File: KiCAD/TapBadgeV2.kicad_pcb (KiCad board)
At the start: 4 copper layers, 44 x 52.4 mm, 83 parts, among them J201 Conn_02x04_Counter_Clockwise, J301 UJC-HP-3-SMT-TR, M101 G0832013D, SW302 KXT 331 LHS, U101 DRV2605, U201 ESP32-PICO-D4, U401 BME680, U402 APDS-9500, U403 LSM6DSM, U404 CMM-4030D-261-I2S-TR, U405 TSOP75340TTCT-ND, U406 MAX86150EFF+T, U407 VL6180XV0NR_1, U408 LP5907MFX-2.8

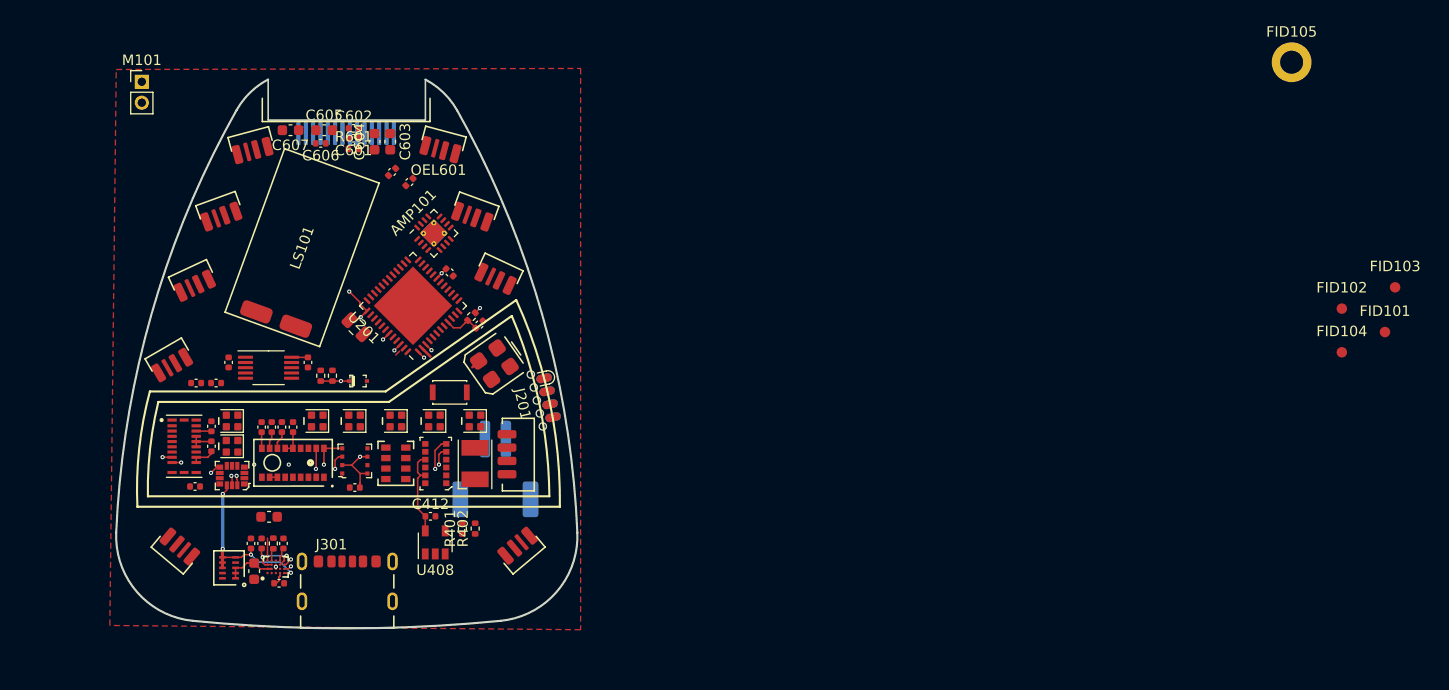
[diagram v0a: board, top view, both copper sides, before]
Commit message: Continue work on Schematics
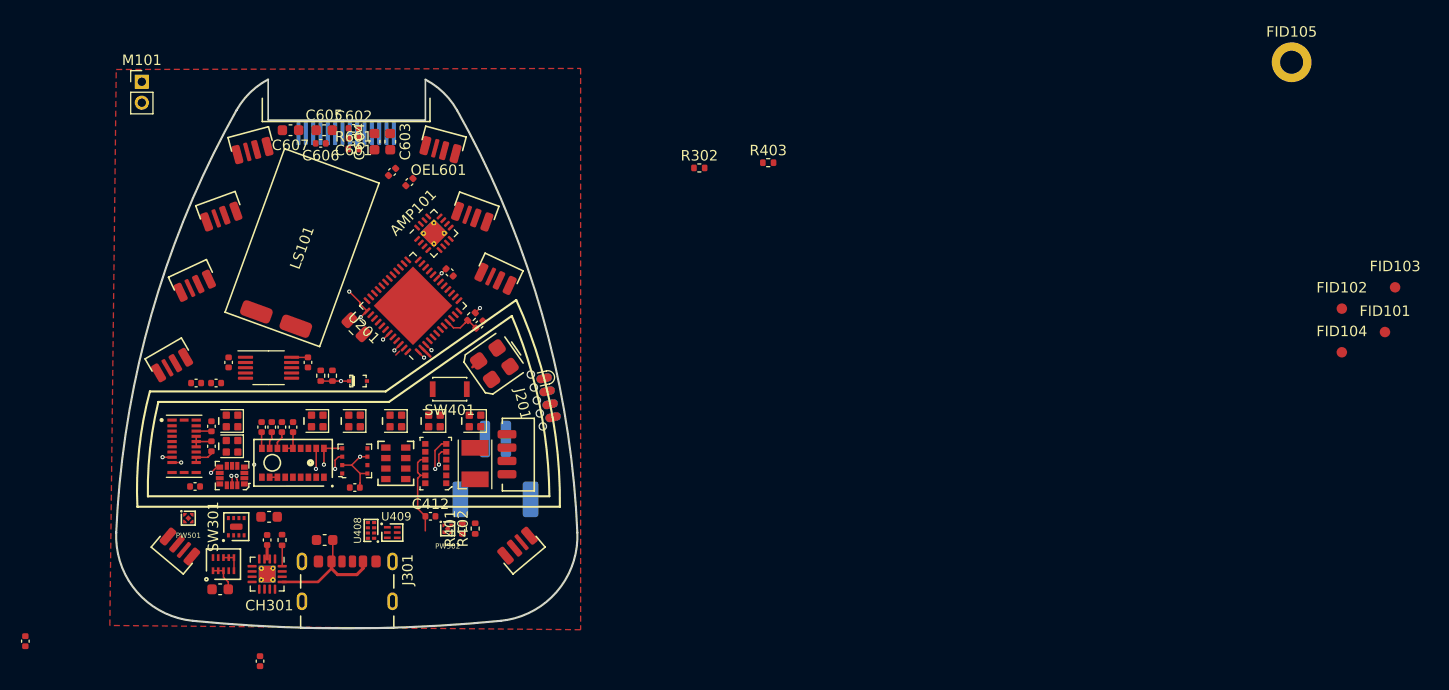
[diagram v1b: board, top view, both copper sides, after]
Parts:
- removed BC301: BQ25157, XasPrints:DSBGA-20
- removed FID301: Fiducial, XasPrints:LiPo_150mAh
- removed SW302: KXT 331 LHS, Button_Switch_SMD:SW_SPST_CK_KXT3
- added CH301: BQ24232, Package_DFN_QFN:VQFN-16-1EP_3x3mm_P0.5mm_EP1.6x1.6mm_ThermalVias, F.Cu at (92.4, 106.3)
- added PW501: AP7354-18FS4, XasPrints:X2-DFN1010-4, F.Cu at (84.9, 101.0)
- added PW502: AP7354-28FS4, XasPrints:X2-DFN1010-4, F.Cu at (109.6, 102.0)
- added R302: 10k 0402, Resistor_SMD:R_0402_1005Metric, F.Cu at (133.6, 67.6)
- added R403: 900k 0402, Resistor_SMD:R_0402_1005Metric, F.Cu at (140.2, 67.1)
- added SW301: MIC94069, XasPrints:MLF-6-EP-P0.5mm, F.Cu at (89.5, 101.8)
- added SW401: KXT 331 LHS, Button_Switch_SMD:SW_SPST_CK_KXT3, F.Cu at (109.8, 88.7)
- added U409: SR1PBBU, XasPrints:UDFN6, F.Cu at (104.3, 102.3)
- C303: value 2.2uF 0402 -> 1uF 0603 16V; footprint Capacitor_SMD:C_0402_1005Metric -> Capacitor_SMD:C_0603_1608Metric
- R301: value 5k 0402 -> 10k 0402
- U408: value LP5907MFX-2.8 -> 74LVC1G74GT-Q100X; footprint Package_TO_SOT_SMD:SOT-23-5 -> XasPrints:XSON8
- moved C305 23.5 mm to (69.3, 112.7), turned to 270 degrees
- moved C304 11.4 mm to (91.7, 114.6)
- moved U408 6.23 mm to (102.3, 102.1)
- moved C303 6.00 mm to (97.9, 103.0), turned to 180 degrees
- moved C302 3.68 mm to (87.9, 107.8), turned to 180 degrees
- moved R301 0.89 mm to (93.8, 103.0)
- moved PW301 0.63 mm to (88.2, 105.4), turned to 0 degrees
- moved C301 0.62 mm to (92.4, 103.0)
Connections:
- net +1V8 renamed Net-(C408-Pad1)
- C101 pad 2: +BATT -> +5V
- C302 pad 1: +BATT -> +5V
- C303 pad 1: Net-(BC301-PadD1) -> Net-(C303-Pad1)
- C304 pad 1: VGLOW -> Net-(C304-Pad1)
- C304 pad 2: GND -> Net-(C304-Pad2)
- J301 pad 2: Net-(BC301-PadA1) -> Net-(C303-Pad1)
- PW301 pad 1: +BATT -> +5V
- PW301 pad 2: +BATT -> +5V
- PW301 pad 3: +BATT -> /Power Handling/MAIN_PWR_ON
- U101 pad 10: +BATT -> +5V
- U101 pad 6: +BATT -> +5V
- U408 pad 1: +3V3 -> Net-(U408-Pad1)
- U408 pad 2: GND -> Net-(U408-Pad2)
- U408 pad 3: +3V3 -> Net-(U408-Pad2)
- U408 pad 4: Net-(U408-Pad4) -> GND
- U408 pad 5: Net-(C412-Pad1) -> /Power Handling/MAIN_PWR_ON
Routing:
- net +3V3: track 38.8 -> 23.4 mm, vias 15 -> 11
- net Net-(C303-Pad1): track 0.00 -> 12.2 mm
- net SCL: track 44.3 -> 34.3 mm, vias 7 -> 5
- net Net-(BT301-Pad1): track 5.66 -> 1.83 mm, vias 2 -> 0
- net +BATT: track 6.43 -> 2.96 mm
- net GND: track 5.00 -> 2.47 mm, vias 1 -> 0
- net +5V: track 0.00 -> 1.56 mm
- net Net-(BC301-PadD1): track 1.35 -> 0.00 mm
- net VGLOW: track 1.07 -> 0.00 mm
- net Net-(CH301-Pad16): track 0.98 -> 2.00 mm
- net SDA: track 36.4 -> 35.7 mm, vias 6 -> 5

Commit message: Add STM32 base circuit for power control and USB, also a lot of other things
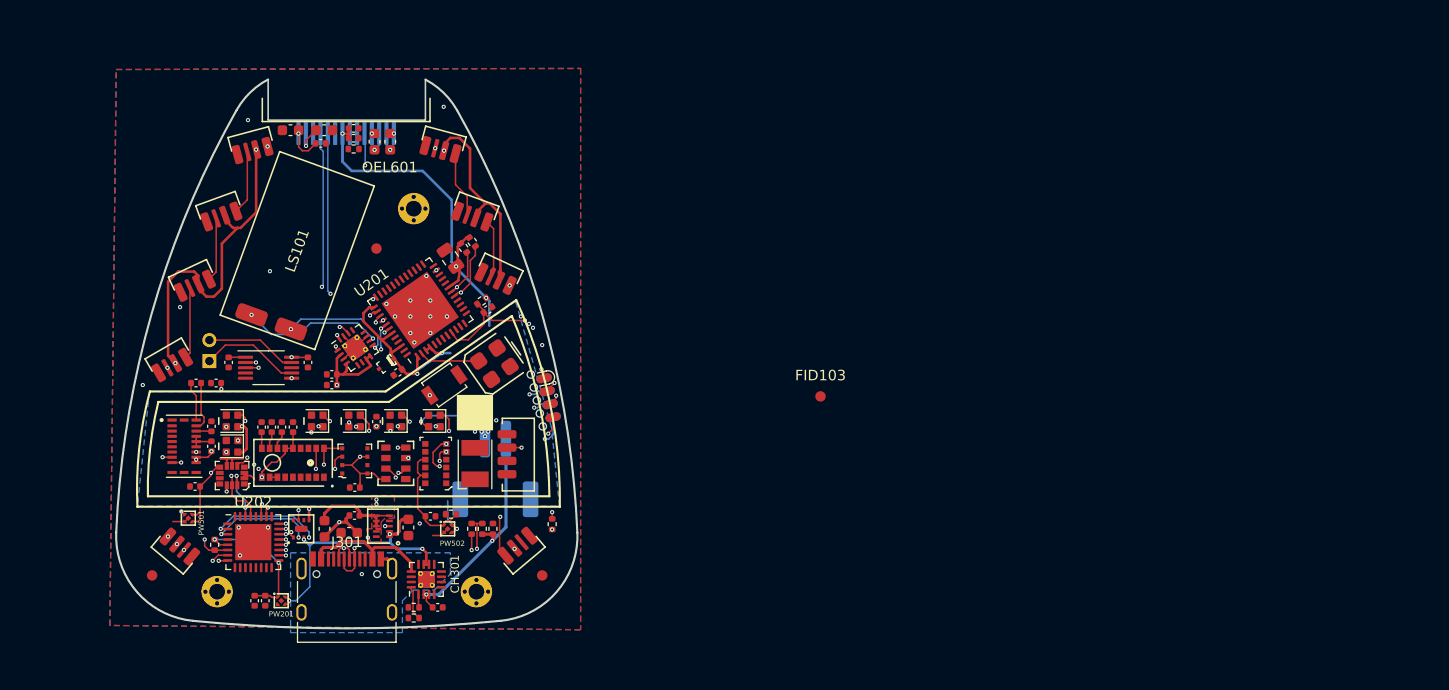
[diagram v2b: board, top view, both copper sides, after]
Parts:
- removed FID105: Fiducial, MountingHole:MountingHole_2.2mm_M2_DIN965_Pad
- removed R403: 900k 0402, Resistor_SMD:R_0402_1005Metric
- removed SW401: KXT 331 LHS, Button_Switch_SMD:SW_SPST_CK_KXT3
- removed U408: 74LVC1G74GT-Q100X, XasPrints:XSON8
- removed U409: SR1PBBU, XasPrints:UDFN6
- added BAT301: SYM_Hot_Small, XasPrints:LiPo_150mAh, B.Cu at (98.3, 90.3)
- added C204: 1uF 0402, Capacitor_SMD:C_0402_1005Metric, F.Cu at (92.2, 108.8)
- added C205: 0.1uF 0402, Capacitor_SMD:C_0402_1005Metric, F.Cu at (91.2, 108.8)
- added H101: MountingHole_Pad, XasPrints:MountingHole_1.5mm_M1_Pad_Via, F.Cu at (87.6, 108.0)
- added H102: MountingHole_Pad, XasPrints:MountingHole_1.5mm_M1_Pad_Via, F.Cu at (112.4, 108.0)
- added H103: MountingHole_Pad, XasPrints:MountingHole_1.5mm_M1_Pad_Via, F.Cu at (106.4, 71.4)
- added PW201: AP7354-33FS4, XasPrints:X2-DFN1010-4, F.Cu at (93.7, 108.8)
- added R202: 10k 0402, Resistor_SMD:R_0402_1005Metric, F.Cu at (87.4, 103.5)
- added R203: 0402 100k, Resistor_SMD:R_0402_1005Metric, F.Cu at (112.9, 102.0)
- added R204: 0402 33k, Resistor_SMD:R_0402_1005Metric, F.Cu at (111.9, 102.0)
- added R205: 0402 10k, Resistor_SMD:R_0402_1005Metric, F.Cu at (119.6, 101.5)
- added SW201: SW_Push, Button_Switch_SMD:SW_SPST_B3U-1000P, F.Cu at (109.3, 88.3)
- added U202: STM32L052K8Ux, Package_DFN_QFN:QFN-32-1EP_5x5mm_P0.5mm_EP3.45x3.45mm, F.Cu at (91.1, 103.3)
- C305: value 2.2uF 0402 -> 0.1uF 0402
- J301: value UJC-HP-3-SMT-TR -> USB4105-GF-A; footprint XasPrints:UJC-HP-3-SMT-TR -> Connector_USB:USB_C_Receptacle_HRO_TYPE-C-31-M-12
- M101: moved to B.Cu
- moved FID101 119.9 mm to (81.4, 106.4)
- moved FID102 92.3 mm to (102.8, 75.2)
- moved FID104 79.2 mm to (118.6, 106.4)
- moved FID103 55.8 mm to (145.2, 89.3)
- moved R302 50.0 mm to (106.4, 109.5), turned to 180 degrees
- moved C305 33.6 mm to (100.7, 100.7), turned to 180 degrees
- moved M101 27.4 mm to (86.9, 86.0)
- moved C304 25.4 mm to (102.8, 91.8)
- moved C104 20.7 mm to (98.6, 88.3), turned to 180 degrees
- moved C103 20.1 mm to (98.6, 87.2), turned to 180 degrees
- moved R102 19.3 mm to (112.0, 74.6), turned to 305 degrees
- moved C302 18.9 mm to (105.9, 101.9), turned to 270 degrees
- moved C301 17.5 mm to (108.7, 109.5), turned to 0 degrees
- moved R101 17.5 mm to (111.1, 75.2), turned to 305 degrees
- moved PW301 15.6 mm to (103.4, 101.7), turned to 90 degrees
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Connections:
- net Net-(D508-Pad2) renamed /Ring 'o LEDs/LED_OUT
- AMP101 pad 14: SPKR_LRCK -> AUDIO_LRCK
- AMP101 pad 16: SPKR_BCK -> AUDIO_BCK
- BT301 pad 1: Net-(BT301-Pad1) -> RAW_BAT
- C301 pad 1: Net-(BT301-Pad1) -> RAW_BAT
- C303 pad 1: Net-(C303-Pad1) -> VUSB
- C304 pad 1: Net-(C304-Pad1) -> VGLOW
- C304 pad 2: Net-(C304-Pad2) -> GND
- CH301 pad 13: Net-(C303-Pad1) -> VUSB
- CH301 pad 2: Net-(BT301-Pad1) -> RAW_BAT
- CH301 pad 3: Net-(BT301-Pad1) -> RAW_BAT
- D201 pad 1: +BATT -> +5V
- D201 pad 2: /Core Schematic/LED_OUT -> /Sensors/LED_IN
- D401 pad 1: Net-(D401-Pad1) -> VGLOW
- D401 pad 3: Net-(D401-Pad3) -> GND
- D402 pad 1: Net-(D402-Pad1) -> VGLOW
- D402 pad 3: Net-(D402-Pad3) -> GND
- D403 pad 1: Net-(D403-Pad1) -> VGLOW
- D403 pad 2: Net-(D403-Pad2) -> Net-(D402-Pad4)
- D403 pad 3: Net-(D403-Pad3) -> GND
- D403 pad 4: Net-(D403-Pad4) -> Net-(D401-Pad2)
- D404 pad 1: Net-(D404-Pad1) -> VGLOW
- D404 pad 2: Net-(D404-Pad2) -> Net-(D401-Pad4)
- D404 pad 3: Net-(D404-Pad3) -> GND
- D406 pad 1: Net-(D406-Pad1) -> VGLOW
- D406 pad 2: Net-(D406-Pad2) -> /Ring 'o LEDs/LED_IN
- D406 pad 3: Net-(D406-Pad3) -> GND
- D406 pad 4: Net-(D406-Pad4) -> Net-(D402-Pad2)
- D407 pad 1: Net-(D407-Pad1) -> VGLOW
- D407 pad 2: Net-(D407-Pad2) -> Net-(D404-Pad4)
- D407 pad 3: Net-(D407-Pad3) -> GND
- D407 pad 4: Net-(D407-Pad4) -> /Sensors/LED_IN
- D501 pad 1: Net-(D501-Pad1) -> VGLOW
- D501 pad 3: Net-(D501-Pad3) -> GND
- D502 pad 1: Net-(D502-Pad1) -> VGLOW
- D502 pad 2: Net-(D502-Pad2) -> Net-(D501-Pad4)
- D502 pad 3: Net-(D502-Pad3) -> GND
- D503 pad 1: Net-(D503-Pad1) -> VGLOW
- D503 pad 2: Net-(D503-Pad2) -> Net-(D502-Pad4)
- D503 pad 3: Net-(D503-Pad3) -> GND
- D504 pad 1: Net-(D504-Pad1) -> VGLOW
- D504 pad 2: Net-(D504-Pad2) -> Net-(D503-Pad4)
- D504 pad 3: Net-(D504-Pad3) -> GND
- D505 pad 1: Net-(D505-Pad1) -> VGLOW
- D505 pad 2: Net-(D505-Pad2) -> Net-(D504-Pad4)
- D505 pad 3: Net-(D505-Pad3) -> GND
- D506 pad 1: Net-(D506-Pad1) -> VGLOW
- D506 pad 2: Net-(D506-Pad2) -> Net-(D505-Pad4)
- D506 pad 3: Net-(D506-Pad3) -> GND
- D507 pad 1: Net-(D507-Pad1) -> VGLOW
- D507 pad 2: Net-(D507-Pad2) -> Net-(D506-Pad4)
- D507 pad 3: Net-(D507-Pad3) -> GND
- D507 pad 4: Net-(D507-Pad4) -> /Ring 'o LEDs/LED_IN
- D508 pad 1: Net-(D508-Pad1) -> VGLOW
- D508 pad 3: Net-(D508-Pad3) -> GND
- D509 pad 1: Net-(D509-Pad1) -> VGLOW
- D509 pad 2: Net-(D509-Pad2) -> Net-(D508-Pad4)
- D509 pad 3: Net-(D509-Pad3) -> GND
- D509 pad 4: Net-(D509-Pad4) -> Net-(D501-Pad2)
- J201 pad 4: Net-(J201-Pad4) -> /Core Schematic/STM_SWDIO
- J201 pad 5: Net-(J201-Pad5) -> /Core Schematic/STM_SWCLK
- OEL601 pad 5: Net-(OEL601-Pad5) -> +BATT
- PW301 pad 3: /Power Handling/MAIN_PWR_ON -> MAIN_PWR_ON
- R402 pad 1: +3V3 -> RAW_BAT
- SW301 pad 1: Net-(BT301-Pad1) -> RAW_BAT
- SW301 pad 2: Net-(SW301-Pad2) -> BAT_ON
- SW301 pad 4: Net-(SW301-Pad4) -> GLOW_ON
- U101 pad 4: Net-(U101-Pad4) -> GND
- U201 pad 17: Net-(U201-Pad17) -> SCL
- U201 pad 18: Net-(U201-Pad18) -> SDA
- U201 pad 36: Net-(U201-Pad36) -> AUDIO_LRCK
- U201 pad 38: Net-(U201-Pad38) -> AUDIO_BCK
- U201 pad 39: Net-(U201-Pad39) -> SPKR_DATA
- U201 pad 42: Net-(U201-Pad42) -> MIC_DATA
- U404 pad 3: MIC_LR -> AUDIO_LRCK
- U404 pad 6: MIC_SCK -> AUDIO_BCK
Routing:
- net VGLOW: track 0.00 -> 167.0 mm, vias 0 -> 14
- net +3V3: track 23.4 -> 96.0 mm, vias 11 -> 16
- net SCL: track 34.3 -> 98.5 mm, vias 5 -> 9
- net SDA: track 35.7 -> 99.4 mm, vias 5 -> 11
- net +5V: track 1.56 -> 63.0 mm, vias 0 -> 7
- net /Core Schematic/BOOT: track 0.00 -> 58.9 mm, vias 0 -> 4
- net /Core Schematic/RESET: track 3.50 -> 57.8 mm, vias 0 -> 3
- net /Core Schematic/E>P: track 0.00 -> 52.9 mm, vias 0 -> 6
- net RAW_BAT: track 0.00 -> 42.4 mm, vias 0 -> 3
- net /Ring 'o LEDs/LED_IN: track 0.00 -> 41.3 mm, vias 0 -> 3
- net +BATT: track 2.96 -> 42.2 mm, vias 0 -> 2
- net Net-(R202-Pad2): track 0.00 -> 37.5 mm, vias 0 -> 3
- net /Core Schematic/STM_SWDIO: track 0.00 -> 37.4 mm, vias 0 -> 2
- net /Core Schematic/STM_SWCLK: track 0.00 -> 37.2 mm, vias 0 -> 2
- net Net-(D508-Pad4): track 0.00 -> 35.6 mm, vias 0 -> 2
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- added copper zone on B.Cu, net +3V3
- added copper zone on F.Cu, net +3V3
- added copper zone on B.Cu, net GND

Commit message: Continue work on TapV2's schematic, almost completing it!
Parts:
- removed FID103: Fiducial, Fiducial:Fiducial_1mm_Mask2mm
- added Q401: DMN3404L, Package_TO_SOT_SMD:SOT-23, F.Cu at (112.7, 101.9)
- added R206: 10k 0402, Resistor_SMD:R_0402_1005Metric, F.Cu at (87.2, 101.5)
- added R403: 36R 0402, Resistor_SMD:R_0402_1005Metric, F.Cu at (102.4, 78.0)
- C103: value 10uF 0402 -> 10uF 0603; footprint Capacitor_SMD:C_0402_1005Metric -> Capacitor_SMD:C_0603_1608Metric
- C303, C603, C604: value 1uF 0603 16V -> 1uF 0402 16V; footprint Capacitor_SMD:C_0603_1608Metric -> Capacitor_SMD:C_0402_1005Metric
- C605, C607: value 2.2uF 0603 16V -> 2.2uF 0402 16V; footprint Capacitor_SMD:C_0603_1608Metric -> Capacitor_SMD:C_0402_1005Metric
- moved R402 11.5 mm to (115.0, 90.6), turned to 180 degrees
- moved R601 3.20 mm to (97.5, 66.3)
- moved R204 2.67 mm to (112.0, 104.6), turned to 135 degrees
- moved R203 2.63 mm to (113.3, 104.6), turned to 135 degrees
- moved C103 2.61 mm to (101.1, 88.1), turned to 0 degrees
- moved C605 0.39 mm to (97.5, 64.1)
- moved C607 0.31 mm to (94.4, 64.1)
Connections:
- H101 pad 1: Net-(H101-Pad1) -> GND
- H102 pad 1: Net-(H102-Pad1) -> GND
- H103 pad 1: Net-(H103-Pad1) -> GND
- J201 pad 8: Net-(J201-Pad8) -> /Core Schematic/STM_RST
- OEL601 pad 9: Net-(OEL601-Pad9) -> +3V3
- U101 pad 5: Net-(U101-Pad5) -> +5V
- U201 pad 14: Net-(U201-Pad14) -> /Core Schematic/STATE_LED
- U201 pad 34: Net-(U201-Pad34) -> IR_TX
- U201 pad 35: Net-(U201-Pad35) -> IR_RX
- U202 pad 1: Net-(U202-Pad1) -> Net-(C204-Pad1)
- U202 pad 10: Net-(U202-Pad10) -> CAM_CS
- U202 pad 11: Net-(U202-Pad11) -> CAM_DCLK
- U202 pad 12: Net-(U202-Pad12) -> CAM_PILOT_CLOCK
- U202 pad 13: Net-(U202-Pad13) -> CAM_DATA
- U202 pad 31: Net-(U202-Pad31) -> GND
- U202 pad 4: Net-(U202-Pad1) -> /Core Schematic/STM_RST
- U405 pad 3: Net-(U405-Pad3) -> IR_RX
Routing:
- net /Core Schematic/STM_RST: track 0.00 -> 53.2 mm, vias 0 -> 3
- net Net-(Q401-Pad1): track 0.00 -> 38.2 mm, vias 0 -> 3
- net IR_RX: track 0.00 -> 29.6 mm, vias 0 -> 3
- net CAM_CS: track 0.00 -> 16.8 mm, vias 0 -> 2
- net CAM_PILOT_CLOCK: track 0.00 -> 15.5 mm, vias 0 -> 2
- net GND: track 24.7 -> 39.9 mm, vias 24 -> 25
- net CAM_DCLK: track 0.00 -> 14.3 mm, vias 0 -> 2
- net CAM_DATA: track 0.00 -> 13.3 mm, vias 0 -> 2
- net /Core Schematic/STATE_LED: track 0.00 -> 13.0 mm, vias 0 -> 2
- net Net-(R401-Pad2): track 0.00 -> 6.07 mm
- net Net-(D408-Pad2): track 0.00 -> 5.57 mm
- net RAW_BAT: track 42.4 -> 47.4 mm, vias 3 -> 4
- net Net-(OEL601-Pad12): track 0.00 -> 4.75 mm, vias 0 -> 1
- net Net-(D408-Pad1): track 0.00 -> 3.78 mm
- net +5V: track 63.0 -> 66.2 mm
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- added copper zone on In1.Cu, net GND
- added copper zone on In2.Cu, net GND

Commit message: Finalize PCB schematics
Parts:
- added C413: 0.1uF 0402, Capacitor_SMD:C_0402_1005Metric, F.Cu at (94.3, 90.7)
- added C414: 0.1uF 0402, Capacitor_SMD:C_0402_1005Metric, F.Cu at (115.8, 101.4)
- added C608: 0.1uF 0402, Capacitor_SMD:C_0402_1005Metric, F.Cu at (109.1, 68.4)
- added J202: Conn_01x04_Female, Connector_PinHeader_1.27mm:PinHeader_1x04_P1.27mm_Vertical, B.Cu at (103.8, 75.1)
- added JP201: SolderJumper_3_Bridged12, Jumper:SolderJumper-3_P1.3mm_Open_RoundedPad1.0x1.5mm, B.Cu at (86.1, 98.7)
- added JP302: SolderJumper_3_Bridged12, Jumper:SolderJumper-3_P1.3mm_Open_RoundedPad1.0x1.5mm, B.Cu at (105.7, 100.8)
- added JP303: SolderJumper_3_Bridged12, Jumper:SolderJumper-3_P1.3mm_Open_RoundedPad1.0x1.5mm, B.Cu at (96.7, 98.8)
- added R207: 36R 0402, Resistor_SMD:R_0402_1005Metric, F.Cu at (110.4, 91.0)
- added R208: 10k 0402, Resistor_SMD:R_0402_1005Metric, F.Cu at (106.0, 90.0)
- added R404: 100R 0402, Resistor_SMD:R_0402_1005Metric, F.Cu at (115.8, 100.6)
- added SYM101: SYM_Radioactive_Large, XasPrints:DragonIcon_7mm_Solder, B.Cu at (93.5, 72.2)
- added TP301: TestPoint, Connector_PinHeader_1.27mm:PinHeader_1x01_P1.27mm_Vertical, B.Cu at (105.6, 104.7)
- moved FID102 3.84 mm to (99.0, 74.7)
- moved U404 0.15 mm to (104.7, 94.4)
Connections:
- AMP101 pad 2: VGLOW -> +5V
- AMP101 pad 7: VGLOW -> +5V
- AMP101 pad 8: VGLOW -> +5V
- C103 pad 1: VGLOW -> +5V
- C104 pad 1: VGLOW -> +5V
- CH301 pad 7: Net-(CH301-Pad7) -> ~VUSB_PRESENT
- CH301 pad 9: Net-(CH301-Pad9) -> ~CHG
- D201 pad 4: /Core Schematic/STATE_LED -> Net-(D201-Pad4)
- PW301 pad 3: MAIN_PWR_ON -> Net-(JP302-Pad2)
- SW301 pad 2: BAT_ON -> Net-(JP303-Pad2)
- U201 pad 12: Net-(U201-Pad12) -> KNOCK_INT
- U201 pad 14: /Core Schematic/STATE_LED -> Net-(R207-Pad2)
- U201 pad 15: Net-(U201-Pad15) -> AUDIO_LRCK
- U201 pad 16: Net-(U201-Pad16) -> IR_RX
- U201 pad 18: SDA -> MIC_DATA
- U201 pad 20: Net-(U201-Pad20) -> /Core Schematic/EXT_1
- U201 pad 21: Net-(U201-Pad21) -> /Core Schematic/EXT_2
- U201 pad 24: Net-(U201-Pad24) -> /Core Schematic/ESP_GLOW_ON
- U201 pad 35: IR_RX -> Net-(U201-Pad35)
- U201 pad 36: AUDIO_LRCK -> Net-(U201-Pad36)
- U201 pad 42: MIC_DATA -> SDA
- U202 pad 14: Net-(U202-Pad14) -> ~VUSB_PRESENT
- U202 pad 16: Net-(U202-Pad16) -> ~CHG
- U202 pad 2: GLOW_ON -> /Core Schematic/STM_GLOW
- U402 pad 2: Net-(U402-Pad2) -> KNOCK_INT
- U403 pad 1: Net-(U403-Pad1) -> GND
- U403 pad 4: Net-(U403-Pad4) -> KNOCK_INT
- U405 pad 2: +3V3 -> Net-(C414-Pad2)
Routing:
- net /Core Schematic/ESP_GLOW_ON: track 0.00 -> 42.4 mm, vias 0 -> 3
- net KNOCK_INT: track 0.00 -> 39.6 mm, vias 0 -> 5
- net ~VUSB_PRESENT: track 0.00 -> 21.2 mm, vias 0 -> 2
- net ~CHG: track 0.00 -> 19.7 mm, vias 0 -> 2
- net /Core Schematic/STATE_LED: track 13.0 -> 0.00 mm, vias 2 -> 0
- net +5V: track 66.2 -> 78.9 mm
- net Net-(R207-Pad2): track 0.00 -> 12.6 mm, vias 0 -> 2
- net IR_RX: track 29.6 -> 20.2 mm, vias 3 -> 2
- net AUDIO_LRCK: track 26.5 -> 35.8 mm, vias 3 -> 4
- net Net-(C414-Pad2): track 0.00 -> 8.98 mm
- net MIC_DATA: track 13.9 -> 21.0 mm, vias 2 -> 3
- net +3V3: track 96.4 -> 103.5 mm, vias 16 -> 17
- net /Core Schematic/STM_GLOW: track 0.00 -> 6.69 mm, vias 0 -> 1
- net Net-(JP303-Pad2): track 0.00 -> 6.60 mm, vias 0 -> 2
- net /Core Schematic/EXT_1: track 0.00 -> 6.15 mm, vias 0 -> 1
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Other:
- board text added: "3V3 S <> ON"
- board text added: "AIR-Q"
- board text added: "BAT BRDG"
- board text added: "G 3 A B"
- board text added: "GESTR"
- board text added: "GLOW E <> S"
- board text added: "GYR"
- board text added: "MIC TOF"
- board text added: "POXY"
- board text added: "STATE"
- board text added: "TapV2 Rev 1.0 Neira, 2021"
